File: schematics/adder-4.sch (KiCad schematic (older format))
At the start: 0 parts

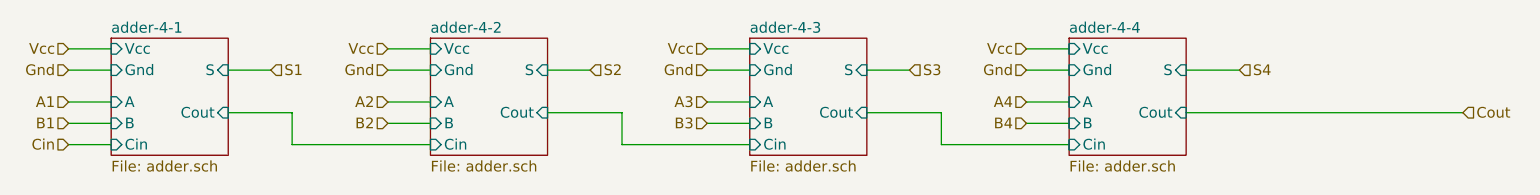
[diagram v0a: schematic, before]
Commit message: Fleshes out basic schematics and some utility software
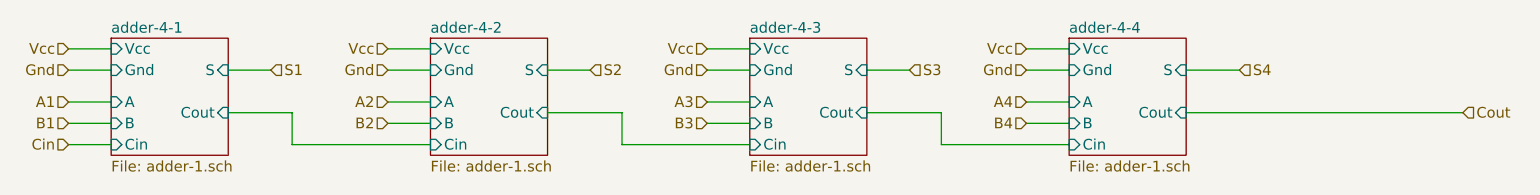
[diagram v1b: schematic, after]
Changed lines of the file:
@@
 $Descr A4 11693 8268
 encoding utf-8
-Sheet 2 225
+Sheet 2 42
 Title ""
 Date ""
@@
 U 5C3B3FDE
 F0 "adder-4-1" 50
-F1 "adder.sch" 50
+F1 "adder-1.sch" 50
 F2 "Vcc" I L 1200 1700 50
 F3 "Gnd" I L 1200 1800 50
@@
 U 5C3B3FE8
 F0 "adder-4-2" 50
-F1 "adder.sch" 50
+F1 "adder-1.sch" 50
 F2 "Vcc" I L 2700 1700 50
 F3 "Gnd" I L 2700 1800 50
@@
 U 5C3B3FF2
 F0 "adder-4-3" 50
-F1 "adder.sch" 50
+F1 "adder-1.sch" 50
 F2 "Vcc" I L 4200 1700 50
 F3 "Gnd" I L 4200 1800 50
@@
 U 5C3B3FFC
 F0 "adder-4-4" 50
-F1 "adder.sch" 50
+F1 "adder-1.sch" 50
 F2 "Vcc" I L 5700 1700 50
 F3 "Gnd" I L 5700 1800 50
